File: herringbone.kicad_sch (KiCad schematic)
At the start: 91 parts, among them U1 ATmega328P-PU, Y1 16MHz

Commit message: Second TRRS jack
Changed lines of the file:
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@@
 	)
 	(junction
-		(at 140.97 77.47)
-		(diameter 0)
-		(color 0 0 0 0)
-	)
-	(junction
 		(at 234.95 82.55)
 		(diameter 0)
@@
 	)
 	(junction
-		(at 144.78 46.99)
-		(diameter 0)
-		(color 0 0 0 0)
-	)
-	(junction
 		(at 67.31 54.61)
 		(diameter 0)
@@
 	(wire
 		(pts
-			(xy 140.97 54.61) (xy 140.97 77.47)
-		)
-		(stroke
-			(width 0)
-			(type default)
-		)
-	)
-	(wire
-		(pts
 			(xy 156.21 116.84) (xy 156.21 120.65)
 		)
@@
 	(wire
 		(pts
+			(xy 140.97 54.61) (xy 140.97 59.69)
+		)
+		(stroke
+			(width 0)
+			(type default)
+		)
+	)
+	(wire
+		(pts
 			(xy 138.43 67.31) (xy 149.86 67.31)
 		)
@@
 	(wire
 		(pts
-			(xy 144.78 69.85) (xy 144.78 46.99)
-		)
-		(stroke
-			(width 0)
-			(type default)
-		)
-	)
-	(wire
-		(pts
 			(xy 118.11 127) (xy 91.44 127)
 		)
@@
 	(wire
 		(pts
+			(xy 144.78 69.85) (xy 144.78 60.96)
+		)
+		(stroke
+			(width 0)
+			(type default)
+		)
+	)
+	(wire
+		(pts
 			(xy 118.11 134.62) (xy 118.11 138.43)
 		)
@@
 	)
 	(symbol
+		(lib_id "torn_left-rescue:GND-power")
+		(at 140.97 59.69 0)
+		(unit 1)
+		(exclude_from_sim no)
+		(in_bom yes)
+		(on_board yes)
+		(dnp no)
+		(property "Reference" "#PWR018"
+			(at 140.97 66.04 0)
+			(effects
+				(font
+					(size 1.27 1.27)
+				)
+				(hide yes)
+			)
+		)
+		(property "Value" "GND"
+			(at 141.097 64.0842 0)
+			(effects
+				(font
+					(size 1.27 1.27)
+				)
+			)
+		)
+		(property "Footprint" ""
+			(at 140.97 59.69 0)
+			(effects
+				(font
+					(size 1.27 1.27)
+				)
+				(hide yes)
+			)
+		)
+		(property "Datasheet" ""
+			(at 140.97 59.69 0)
+			(effects
+				(font
+					(size 1.27 1.27)
+				)
+				(hide yes)
+			)
+		)
+		(property "Description" ""
+			(at 140.97 59.69 0)
+			(effects
+				(font
+					(size 1.27 1.27)
+				)
+			)
+		)
+		(pin "1"
+		)
+		(instances
+			(project "herringbone"
+				(path "/44dd7199-56c3-4a99-8ba5-a286c9c8aec3"
+					(reference "#PWR018")
+					(unit 1)
+				)
+			)
+		)
+	)
+	(symbol
 		(lib_id "ScottoKeebs:Placeholder_Keyswitch")
 		(at 248.92 44.45 0)
@@
 					(unit 1)
 				)
+			)
+		)
+	)
+	(symbol
+		(lib_id "power:+5V")
+		(at 144.78 60.96 0)
+		(unit 1)
+		(exclude_from_sim no)
+		(in_bom yes)
+		(on_board yes)
+		(dnp no)
+		(fields_autoplaced yes)
+		(property "Reference" "#PWR09"
+			(at 144.78 64.77 0)
+			(effects
+				(font
+					(size 1.27 1.27)
+				)
+				(hide yes)
+			)
+		)
+		(property "Value" "+5V"
+			(at 144.78 55.88 0)
+			(effects
+				(font
+					(size 1.27 1.27)
+				)
+			)
+		)
+		(property "Footprint" ""
+			(at 144.78 60.96 0)
+			(effects
+				(font
+					(size 1.27 1.27)
+				)
+				(hide yes)
+			)
+		)
+		(property "Datasheet" ""
+			(at 144.78 60.96 0)
+			(effects
+				(font
+					(size 1.27 1.27)
+				)
+				(hide yes)
+			)
+		)
+		(property "Description" "Power symbol creates a global label with name \"+5V\""
+			(at 144.78 60.96 0)
+			(effects
+				(font
+					(size 1.27 1.27)
+				)
+				(hide yes)
+			)
+		)
+		(pin "1"
+		)
+		(instances
+			(project "herringbone"
+				(path "/44dd7199-56c3-4a99-8ba5-a286c9c8aec3"
+					(reference "#PWR09")
+					(unit 1)
+				)

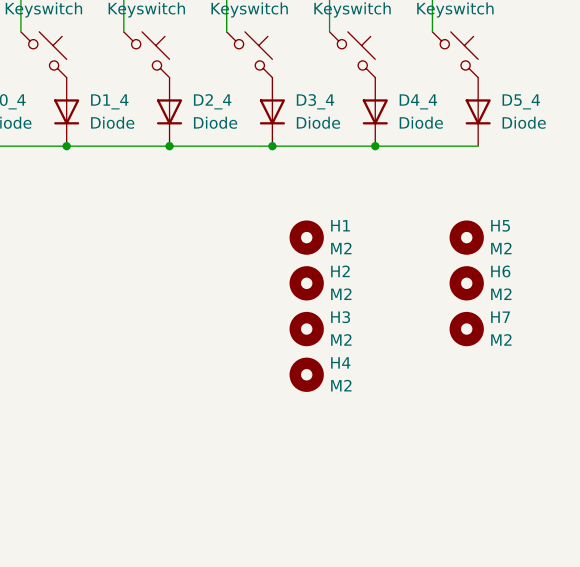
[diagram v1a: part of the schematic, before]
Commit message: Add plate and bottom.
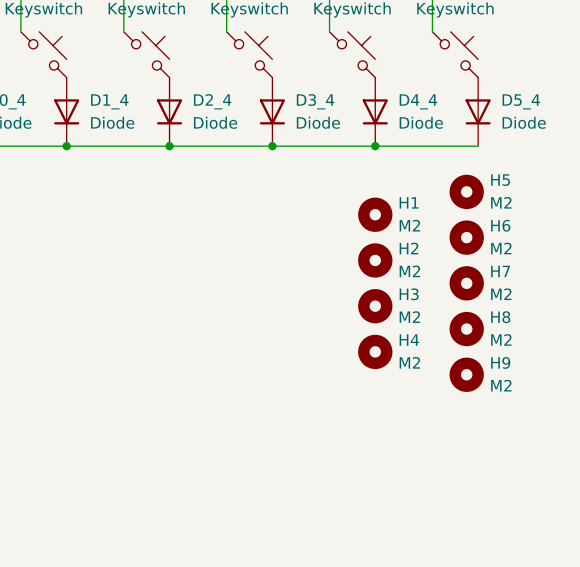
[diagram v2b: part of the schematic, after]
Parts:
- added H8, H9: M2, MountingHole:MountingHole_2.2mm_M2_Pad, symbol Mechanical:MountingHole
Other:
- moved on the sheet: H1, H2, H3, H4, H5, H6, H7
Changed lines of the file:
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@@
 	(symbol
 		(lib_id "Mechanical:MountingHole")
-		(at 261.62 146.05 0)
+		(at 261.62 140.97 0)
 		(unit 1)
 		(exclude_from_sim no)
@@
 		(fields_autoplaced yes)
 		(property "Reference" "H5"
-			(at 264.16 144.7799 0)
+			(at 264.16 139.6999 0)
 			(effects
 				(font
@@
 		)
 		(property "Value" "M2"
-			(at 264.16 147.3199 0)
+			(at 264.16 142.2399 0)
 			(effects
 				(font
@@
 		)
 		(property "Footprint" "MountingHole:MountingHole_2.2mm_M2_Pad"
-			(at 261.62 146.05 0)
+			(at 261.62 140.97 0)
 			(effects
 				(font
@@
 		)
 		(property "Datasheet" "~"
-			(at 261.62 146.05 0)
+			(at 261.62 140.97 0)
 			(effects
 				(font
@@
 		)
 		(property "Description" "Mounting Hole without connection"
-			(at 261.62 146.05 0)
+			(at 261.62 140.97 0)
 			(effects
 				(font
@@
 	(symbol
 		(lib_id "Mechanical:MountingHole")
-		(at 243.84 156.21 0)
+		(at 251.46 153.67 0)
 		(unit 1)
 		(exclude_from_sim no)
@@
 		(fields_autoplaced yes)
 		(property "Reference" "H3"
-			(at 246.38 154.9399 0)
+			(at 254 152.3999 0)
 			(effects
 				(font
@@
 		)
 		(property "Value" "M2"
-			(at 246.38 157.4799 0)
+			(at 254 154.9399 0)
 			(effects
 				(font
@@
 		)
 		(property "Footprint" "MountingHole:MountingHole_2.2mm_M2_Pad"
-			(at 243.84 156.21 0)
+			(at 251.46 153.67 0)
 			(effects
 				(font
@@
 		)
 		(property "Datasheet" "~"
-			(at 243.84 156.21 0)
+			(at 251.46 153.67 0)
 			(effects
 				(font
@@
 		)
 		(property "Description" "Mounting Hole without connection"
-			(at 243.84 156.21 0)
+			(at 251.46 153.67 0)
 			(effects
 				(font
@@
 	)
 	(symbol
+		(lib_id "Mechanical:MountingHole")
+		(at 261.62 156.21 0)
+		(unit 1)
+		(exclude_from_sim no)
+		(in_bom yes)
+		(on_board yes)
+		(dnp no)
+		(fields_autoplaced yes)
+		(property "Reference" "H8"
+			(at 264.16 154.9399 0)
+			(effects
+				(font
+					(size 1.27 1.27)
+				)
+				(justify left)
+			)
+		)
+		(property "Value" "M2"
+			(at 264.16 157.4799 0)
+			(effects
+				(font
+					(size 1.27 1.27)
+				)
+				(justify left)
+			)
+		)
+		(property "Footprint" "MountingHole:MountingHole_2.2mm_M2_Pad"
+			(at 261.62 156.21 0)
+			(effects
+				(font
+					(size 1.27 1.27)
+				)
+				(hide yes)
+			)
+		)
+		(property "Datasheet" "~"
+			(at 261.62 156.21 0)
+			(effects
+				(font
+					(size 1.27 1.27)
+				)
+				(hide yes)
+			)
+		)
+		(property "Description" "Mounting Hole without connection"
+			(at 261.62 156.21 0)
+			(effects
+				(font
+					(size 1.27 1.27)
+				)
+				(hide yes)
+			)
+		)
+		(instances
+			(project "herringbone"
+				(path "/44dd7199-56c3-4a99-8ba5-a286c9c8aec3"
+					(reference "H8")
+					(unit 1)
+				)
+			)
+		)
+	)
+	(symbol
 		(lib_id "ScottoKeebs:Placeholder_Keyswitch")
 		(at 260.35 44.45 0)
@@
 	(symbol
 		(lib_id "Mechanical:MountingHole")
-		(at 261.62 156.21 0)
+		(at 261.62 151.13 0)
 		(unit 1)
 		(exclude_from_sim no)
@@
 		(fields_autoplaced yes)
 		(property "Reference" "H7"
-			(at 264.16 154.9399 0)
+			(at 264.16 149.8599 0)
 			(effects
 				(font
@@
 		)
 		(property "Value" "M2"
-			(at 264.16 157.4799 0)
+			(at 264.16 152.3999 0)
 			(effects
 				(font
@@
 		)
 		(property "Footprint" "MountingHole:MountingHole_2.2mm_M2_Pad"
-			(at 261.62 156.21 0)
+			(at 261.62 151.13 0)
 			(effects
 				(font
@@
 		)
 		(property "Datasheet" "~"
-			(at 261.62 156.21 0)
+			(at 261.62 151.13 0)
 			(effects
 				(font
@@
 		)
 		(property "Description" "Mounting Hole without connection"
-			(at 261.62 156.21 0)
+			(at 261.62 151.13 0)
 			(effects
 				(font
@@
 	(symbol
 		(lib_id "Mechanical:MountingHole")
-		(at 261.62 151.13 0)
+		(at 261.62 146.05 0)
 		(unit 1)
 		(exclude_from_sim no)
@@
 		(fields_autoplaced yes)
 		(property "Reference" "H6"
-			(at 264.16 149.8599 0)
+			(at 264.16 144.7799 0)
 			(effects
 				(font
@@
 		)
 		(property "Value" "M2"
-			(at 264.16 152.3999 0)
+			(at 264.16 147.3199 0)
 			(effects
 				(font
@@
 		)
 		(property "Footprint" "MountingHole:MountingHole_2.2mm_M2_Pad"
-			(at 261.62 151.13 0)
+			(at 261.62 146.05 0)
 			(effects
 				(font
@@
 		)
 		(property "Datasheet" "~"
-			(at 261.62 151.13 0)
+			(at 261.62 146.05 0)
 			(effects
 				(font
@@
 		)
 		(property "Description" "Mounting Hole without connection"
-			(at 261.62 151.13 0)
+			(at 261.62 146.05 0)
 			(effects
 				(font
@@
 	(symbol
 		(lib_id "Mechanical:MountingHole")
-		(at 243.84 161.29 0)
+		(at 251.46 158.75 0)
 		(unit 1)
 		(exclude_from_sim no)
@@
 		(fields_autoplaced yes)
 		(property "Reference" "H4"
-			(at 246.38 160.0199 0)
+			(at 254 157.4799 0)
 			(effects
 				(font
@@
 		)
 		(property "Value" "M2"
-			(at 246.38 162.5599 0)
+			(at 254 160.0199 0)
 			(effects
 				(font
@@
 		)
 		(property "Footprint" "MountingHole:MountingHole_2.2mm_M2_Pad"
-			(at 243.84 161.29 0)
+			(at 251.46 158.75 0)
 			(effects
 				(font
@@
 		)
 		(property "Datasheet" "~"
-			(at 243.84 161.29 0)
+			(at 251.46 158.75 0)
 			(effects
 				(font
@@
 		)
 		(property "Description" "Mounting Hole without connection"
-			(at 243.84 161.29 0)
+			(at 251.46 158.75 0)
 			(effects
 				(font
@@
 	)
 	(symbol
+		(lib_id "Mechanical:MountingHole")
+		(at 261.62 161.29 0)
+		(unit 1)
+		(exclude_from_sim no)
+		(in_bom yes)
+		(on_board yes)
+		(dnp no)
+		(fields_autoplaced yes)
+		(property "Reference" "H9"
+			(at 264.16 160.0199 0)
+			(effects
+				(font
+					(size 1.27 1.27)
+				)
+				(justify left)
+			)
+		)
+		(property "Value" "M2"
+			(at 264.16 162.5599 0)
+			(effects
+				(font
+					(size 1.27 1.27)
+				)
+				(justify left)
+			)
+		)
+		(property "Footprint" "MountingHole:MountingHole_2.2mm_M2_Pad"
+			(at 261.62 161.29 0)
+			(effects
+				(font
+					(size 1.27 1.27)
+				)
+				(hide yes)
+			)
+		)
+		(property "Datasheet" "~"
+			(at 261.62 161.29 0)
+			(effects
+				(font
+					(size 1.27 1.27)
+				)
+				(hide yes)
+			)
+		)
+		(property "Description" "Mounting Hole without connection"
+			(at 261.62 161.29 0)
+			(effects
+				(font
+					(size 1.27 1.27)
+				)
+				(hide yes)
+			)
+		)
+		(instances
+			(project "herringbone"
+				(path "/44dd7199-56c3-4a99-8ba5-a286c9c8aec3"
+					(reference "H9")
+					(unit 1)
+				)
+			)
+		)
+	)
+	(symbol
 		(lib_id "ScottoKeebs:Placeholder_Diode")
 		(at 251.46 91.44 90)
@@
 	(symbol
 		(lib_id "Mechanical:MountingHole")
-		(at 243.84 146.05 0)
+		(at 251.46 143.51 0)
 		(unit 1)
 		(exclude_from_sim no)
@@
 		(fields_autoplaced yes)
 		(property "Reference" "H1"
-			(at 246.38 144.7799 0)
+			(at 254 142.2399 0)
 			(effects
 				(font
@@
 		)
 		(property "Value" "M2"
-			(at 246.38 147.3199 0)
+			(at 254 144.7799 0)
 			(effects
 				(font
@@
 		)
 		(property "Footprint" "MountingHole:MountingHole_2.2mm_M2_Pad"
-			(at 243.84 146.05 0)
+			(at 251.46 143.51 0)
 			(effects
 				(font
@@
 		)
 		(property "Datasheet" "~"
-			(at 243.84 146.05 0)
+			(at 251.46 143.51 0)
 			(effects
 				(font
@@
 		)
 		(property "Description" "Mounting Hole without connection"
-			(at 243.84 146.05 0)
+			(at 251.46 143.51 0)
 			(effects
 				(font
@@
 	(symbol
 		(lib_id "Mechanical:MountingHole")
-		(at 243.84 151.13 0)
+		(at 251.46 148.59 0)
 		(unit 1)
 		(exclude_from_sim no)
@@
 		(fields_autoplaced yes)
 		(property "Reference" "H2"
-			(at 246.38 149.8599 0)
+			(at 254 147.3199 0)
 			(effects
 				(font
@@
 		)
 		(property "Value" "M2"
-			(at 246.38 152.3999 0)
+			(at 254 149.8599 0)
 			(effects
 				(font
@@
 		)
 		(property "Footprint" "MountingHole:MountingHole_2.2mm_M2_Pad"
-			(at 243.84 151.13 0)
+			(at 251.46 148.59 0)
 			(effects
 				(font
@@
 		)
 		(property "Datasheet" "~"
-			(at 243.84 151.13 0)
+			(at 251.46 148.59 0)
 			(effects
 				(font
@@
 		)
 		(property "Description" "Mounting Hole without connection"
-			(at 243.84 151.13 0)
+			(at 251.46 148.59 0)
 			(effects
 				(font
